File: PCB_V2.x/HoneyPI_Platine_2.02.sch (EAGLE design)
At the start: 76 parts

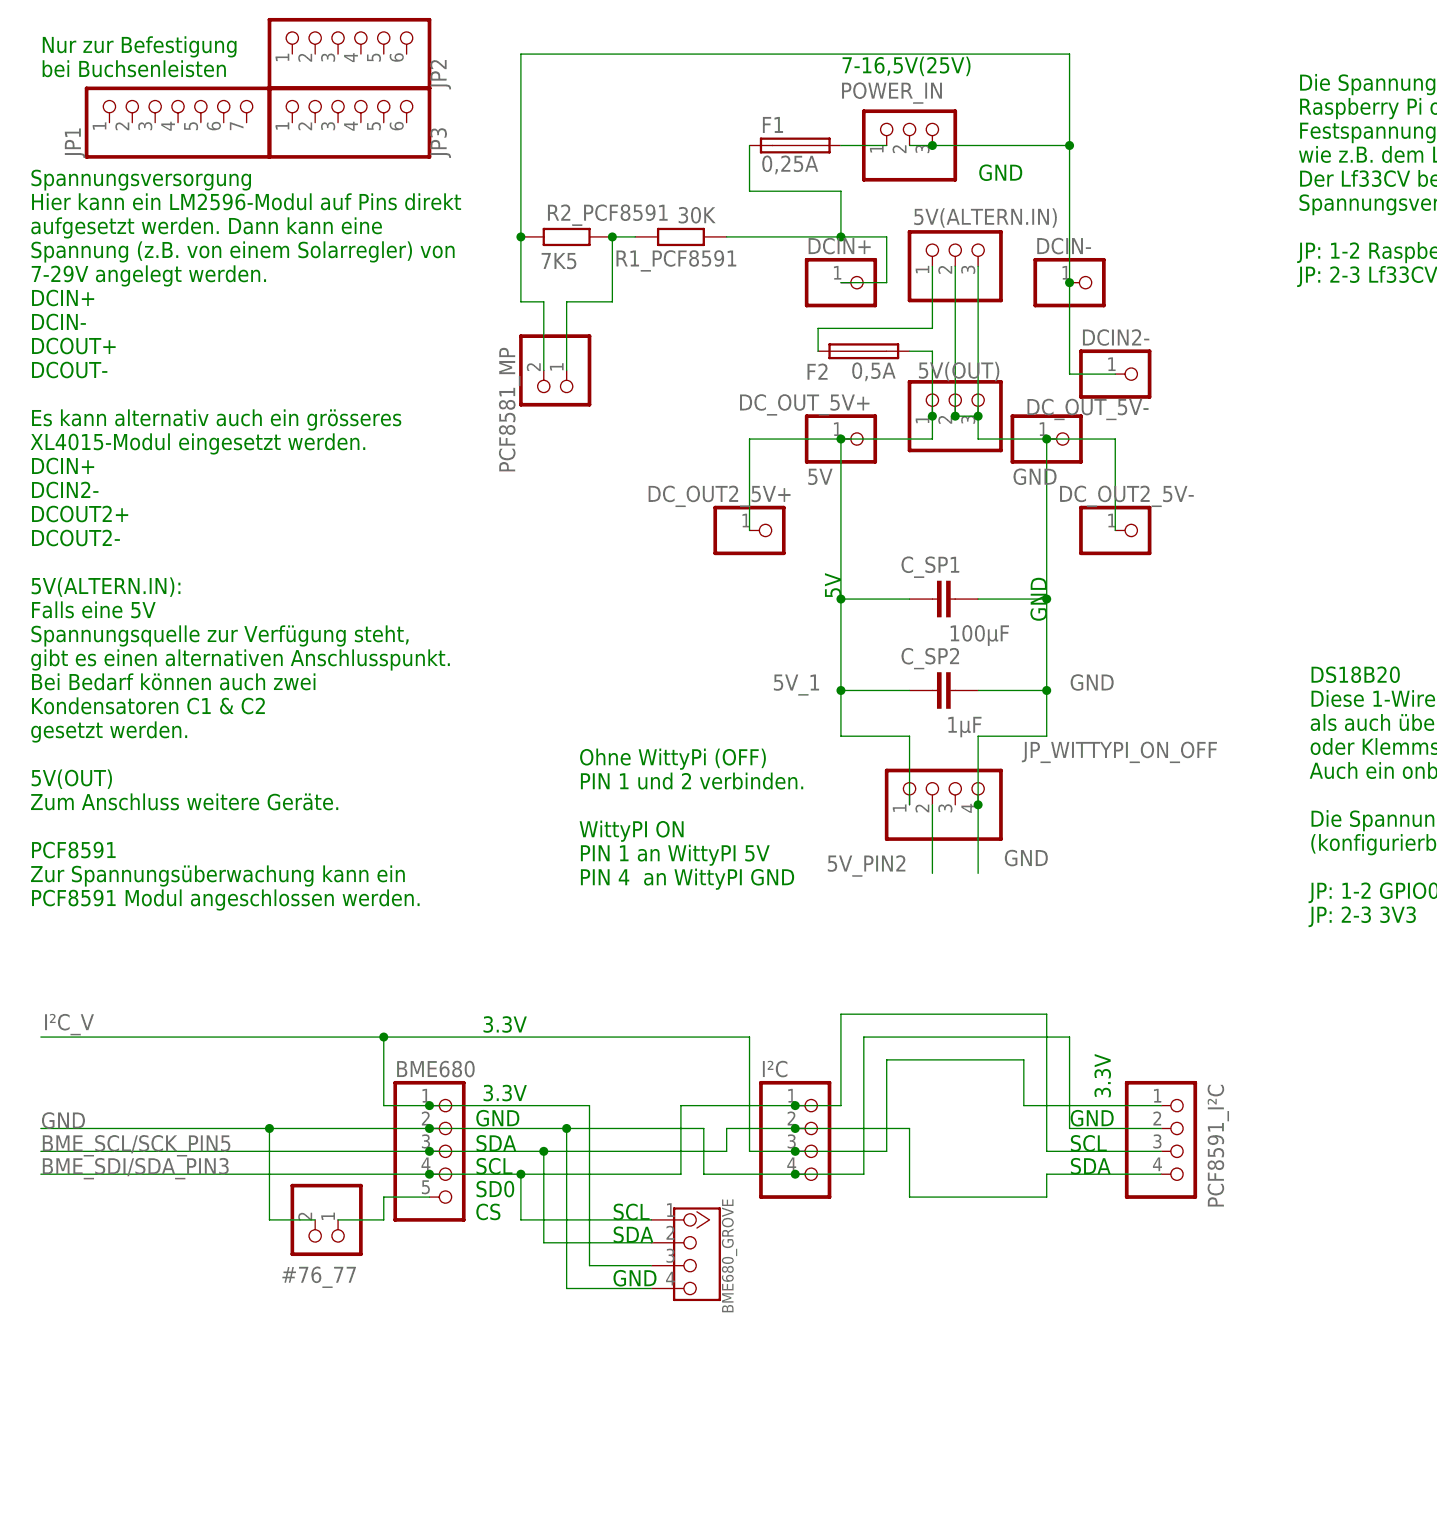
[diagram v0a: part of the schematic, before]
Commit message: New releases
Fix BME680_GROVE Pinout on the main board
Some corrections on the sensor board
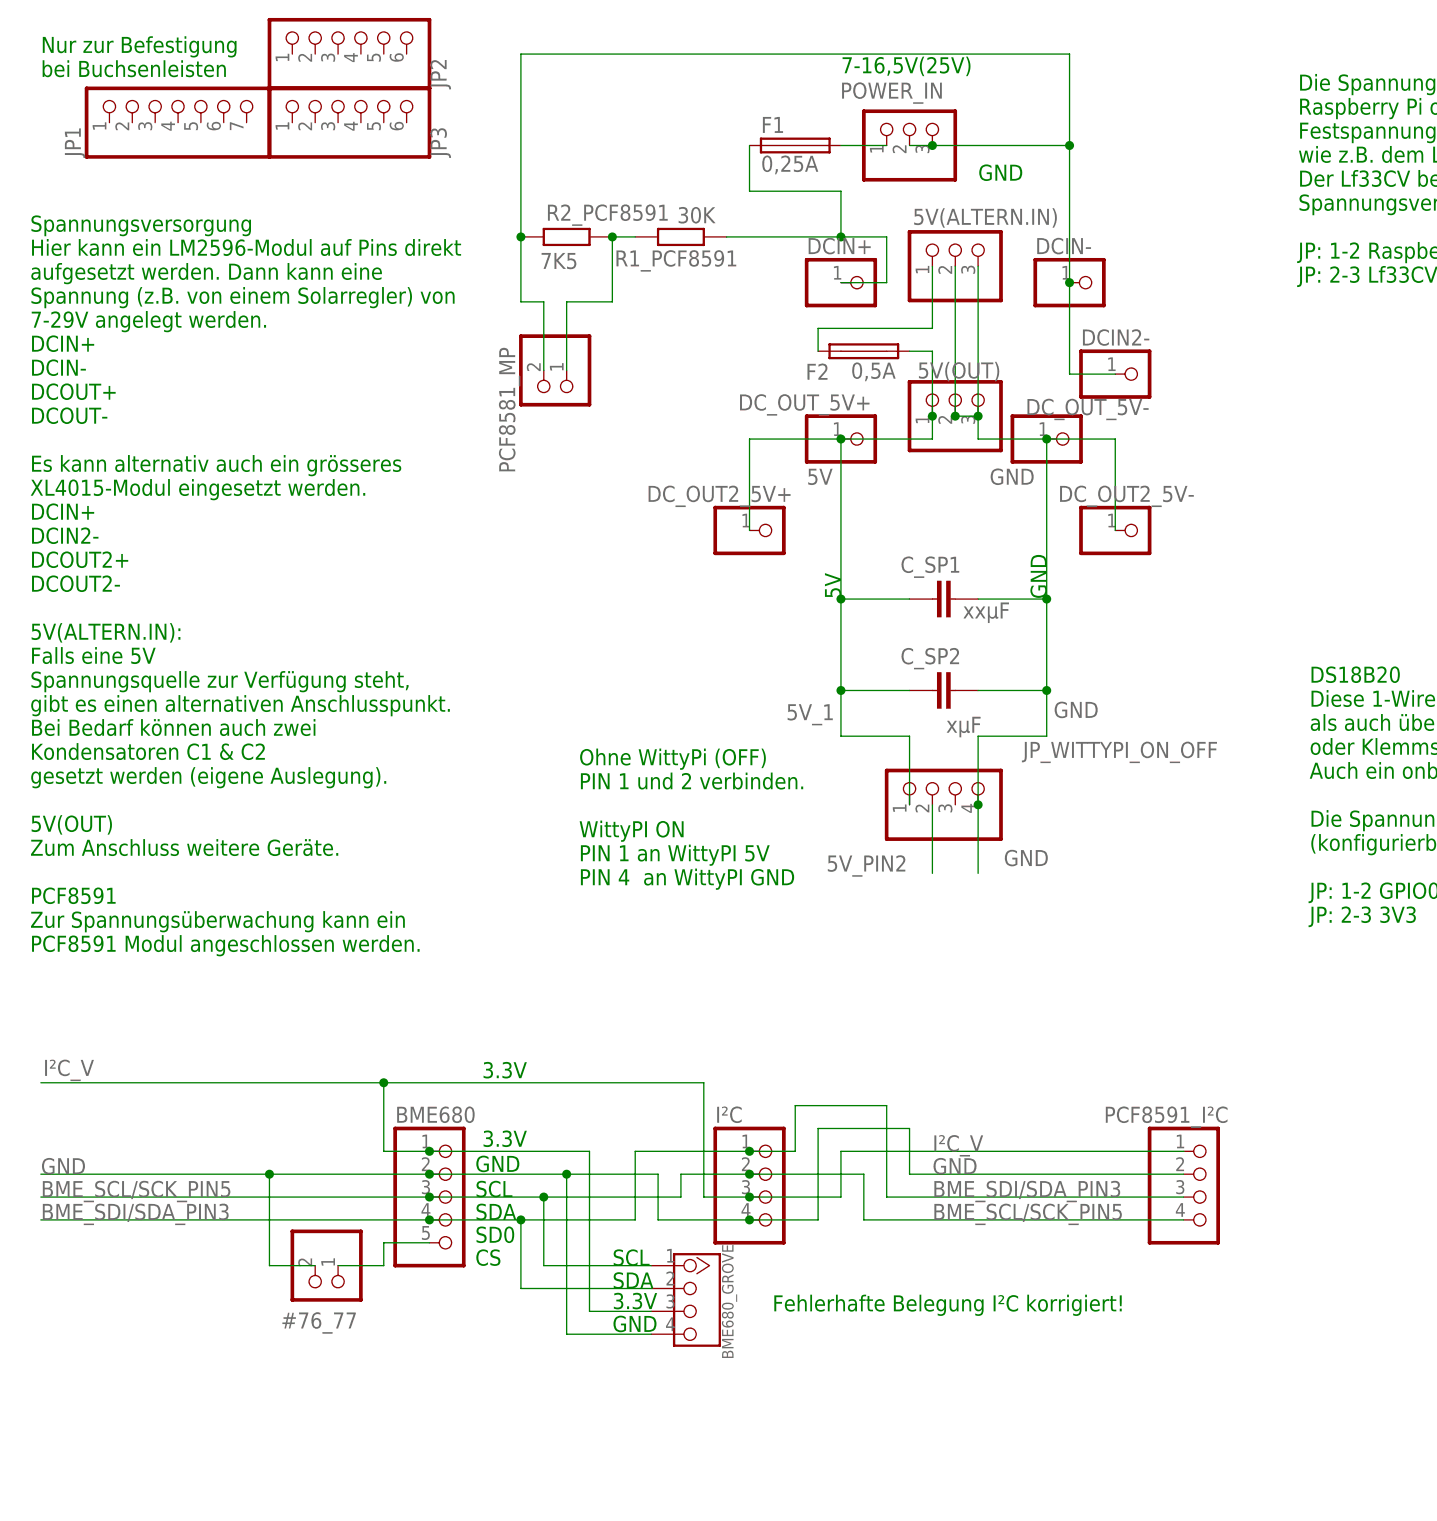
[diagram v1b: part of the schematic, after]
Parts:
- C_SP1: value 100µF -> xxµF
- C_SP2: value 1µF -> xµF
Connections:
- net BME_SCL/SCK_PIN5: now also BME680_GROVE.1; no longer BME680_GROVE.2
- net BME_SDI/SDA_PIN3: now also BME680_GROVE.2; no longer BME680_GROVE.1
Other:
- note added: "Fehlerhafte Belegung I²C korrigiert!"
- moved on the sheet: #76_77, BME680, BME680_GROVE, I²C, PCF8591_I²C
